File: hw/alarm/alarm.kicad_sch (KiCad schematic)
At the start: 23 parts, among them IC1 DS3231S#T&R, IC2 TSOP38238, IC3 SHT40-BD1B-R2, U1 RaspberryPi_Pico, U2 PEC11R-4215F-S0024, U4 HT16K33

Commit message: Reorganize libraries, various updates to schematic
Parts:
- removed D1: RB876WTL, symbol Device:D_Schottky
- removed LED3, LED4: DISP_SEGMENT_STARBURST_DUAL_COMMONCATHODE, Adafruit 0.54 Alphanumeric STEMMA QT:SEGMENT_STARTBUST_DUAL_KWA-541CBB, symbol Adafruit 0.54 Alphanumeric STEMMA QT-eagle-import:DISP_SEGMENT_STARBURST_DUAL_C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
- removed LS1, LS2, LS3: CEM-1203_42_, CEM-1203(42), symbol SamacSys_Parts:CEM-1203_42_
- removed U4: HT16K33, Adafruit 0.54 Alphanumeric STEMMA QT:SOP28_300MIL_SKINNY, symbol Adafruit 0.54 Alphanumeric STEMMA QT-eagle-import:HT16K33_SOP28_SKINNY
- added C10, C12, C16: 4.7uF, Capacitor_SMD:C_0805_2012Metric, symbol Device:C
- added C11, C13, C14, C15, C3, C4, C5, C6, C7, C8, C9: 0.1uF, Capacitor_SMD:C_0805_2012Metric, symbol Device:C
- added D2: LED, LED_SMD:LED_0603_1608Metric, symbol Device:LED
- added D3, D4, D5: MBR0530, Diode_SMD:D_SOD-123, symbol Diode:MBR0530
- added IC4: 23K256-I_SN, SOIC127P600X175-8N, symbol SamacSys_Parts:23K256-I_SN
- added J1: 4328, 4328:ADAFRUIT_4328, symbol 4328:4328
- added J2: SFV24R-4STBE1HLF, SFV24R4STBE1HLF, symbol SamacSys_Parts:SFV24R-4STBE1HLF
- added L1: 10uH, NR4018T100M, symbol SamacSys_Parts:NR4018T100M
- added LS1, LS2, LS3: PT-1241PFQ, PT1241PFQ, symbol SamacSys_Parts:PT-1241PFQ
- added Q1: DMG2305UX-7, SOT96P240X115-3N, symbol SamacSys_Parts:DMG2305UX-7
- added Q2: IRLML2060TRPBF, SOT95P237X112-3N, symbol SamacSys_Parts:IRLML2060TRPBF
- added R3: 267Ω, Resistor_SMD:R_0603_1608Metric_Pad0.98x0.95mm_HandSolder, symbol Device:R
- added U3: 2462, 2462, symbol SamacSys_Parts:2462
- added U4: AS1115-BSST, Package_SO:QSOP-24_3.9x8.7mm_P0.635mm, symbol Interface_Expansion:AS1115-BSST
- added U5: TDCR1060M, TDCG1060M_VIS, symbol 2024-07-15_04-25-04:TDCR1060M
- C1, C2: value 10uF -> 0.1uF; footprint (none) -> Capacitor_SMD:C_0805_2012Metric
- R1: value 10k -> 0.47Ω; footprint (none) -> Resistor_SMD:R_0603_1608Metric_Pad0.98x0.95mm_HandSolder
- R2: value 10k -> 10kΩ; footprint (none) -> Resistor_SMD:R_0603_1608Metric_Pad0.98x0.95mm_HandSolder
- U1: footprint Module_RaspberryPi_Pico:RaspberryPi_Pico_Common -> Module_RaspberryPi_Pico:RaspberryPi_Pico_Original_SMD_MountingHoles_HandSolder_Castellated; symbol MCU_Module_RaspberryPi_Pico:RaspberryPi_Pico -> MCU_Module_RaspberryPi_Pico:RaspberryPi_Pico_DebugPins
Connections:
- net +3.3V: now also IC2.3 (VS), IC3.4 (VSS), C10.2, C14.1, C15.1, C16.1, IC4.7 (~{HOLD}), IC4.8 (VCC), J1.4, J2.15 (VDDIO), J2.16 (VCI), L1.1
- net GND: now also IC2.2 (GND), IC3.3 (VDD), R1.2, R2.2, S2.3, S3.3, S4.3, S5.3, S6.3, S7.1 (COM), U1.D2 (GND), U2.1 (COM), U2.C1 (COMMON), C10.1, C11.1, C13.1, C14.2, C15.2, C16.2, C3.1, C4.1, C5.1, C6.1, C7.1, C8.1, C9.1, D2.1 (K), D3.1 (K), IC4.4 (VSS), J1.3, J2.17 (VSS), J2.8 (BSI), LS1.1 (-), LS2.1 (-), LS3.1 (-), U3.2 (-)
- net SCL: now also IC3.2 (SCL), U1.7 (GPIO5), J1.1; no longer R2.2, U1.27 (GPIO21)
- net SDA: now also IC3.1 (SDA), U1.6 (GPIO4), J1.2; no longer R1.2, U1.29 (GPIO22)
- net at S5.2: now also U1.20 (GPIO15)
- net at S4.2: now also U1.19 (GPIO14)
- net at S6.2: now also U1.15 (GPIO11)
- net at IC2.1 (OUT): now also U1.29 (GPIO22), R3.2
- net at S3.2: now also U1.17 (GPIO13)
- net MOSI: now reaches U1.1 (GPIO0)
- net MOSI: now also IC4.5 (SI), J2.14 (SDIO)
- net EinkCS: now reaches U1.10 (GPIO7)
- net EinkCS: now also J2.12 (CS)
- net Enc_A1: now reaches U1.11 (GPIO8)
- net Enc_A1: now also U2.A1 (CHANNEL_A)
- net Enc_B1: now reaches U1.12 (GPIO9)
- net Enc_B1: now also U2.B1 (CHANNEL_B)
- net at U1.14 (GPIO10): now also U2.2 (NO)
- net at U1.16 (GPIO12): now also S2.2
- net MISO: now reaches U1.2 (GPIO1)
- net MISO: now also IC4.2 (SO)
- net at U1.21 (GPIO16): now also LS3.2 (+)
- net at U1.22 (GPIO17): now also LS2.2 (+)
- net at U1.24 (GPIO18): now also LS1.2 (+)
- net at U1.25 (GPIO19): now also S7.2 (NO)
- net EinkRESET: now reaches U1.26 (GPIO20)
- net EinkRESET: now also J2.10 (RES)
- net at U1.39 (VSYS): now also Q1.2 (S)
- net SCK: now reaches U1.4 (GPIO2)
- net SCK: now also IC4.6 (SCK), J2.13 (SCK)
- net at U1.40 (VBUS): now also Q1.1 (G)
- net DC: now reaches U1.5 (GPIO3)
- net DC: now also J2.11 (D/C)
- net SRAMCS: now reaches U1.9 (GPIO6)
- net SRAMCS: now also IC4.1 (~{CS})
- net GDR: now reaches R2.1
- net GDR: now also J2.2 (GDR), Q2.1 (G); no longer R1.1
- new net: C8.2, J2.5 (VSH2)
- new net: C12.1, D5.2 (A), L1.2, Q2.3 (D)
- new net: C12.2, D3.2 (A), D4.1 (K)
- new net: C3.2, J2.24 (VCOM)
- new net: C6.2, J2.19 (VPP)
- new net: C5.2, J2.20 (VSH1)
- new net: D2.2 (A), R3.1
- new net: Q1.3 (D), U3.1 (+)
- new net: C7.2, J2.18 (VDD)
- new net: C4.2, J2.22 (VSL)
- new net: C9.2, J2.4 (VGL/NC)
- new net: J1.SH1 (SHIELD), J1.SH2 (SHIELD)
- new net EinkBUSY: J2.9 (BUSY), U1.27 (GPIO21)
- new net RESE: J2.3 (RESE), Q2.2 (S), R1.1
- new net VGH: C13.2, D5.1 (K), J2.21 (VGH)
- new net VGL: C11.2, D4.2 (A), J2.23 (VGL)
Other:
- note added: "E-paper"
- note added: "RTC"
- note added: "Temp/Humidity"
- moved on the sheet: IC1, IC2, IC3, S7

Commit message: Add segment display circuit
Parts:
- removed Q2: IRLML2060TRPBF, SOT95P237X112-3N, symbol SamacSys_Parts:IRLML2060TRPBF
- added C17: 0.1uF, Capacitor_SMD:C_0805_2012Metric, symbol Device:C
- added Q3: Si1308EDL-T1-GE3, SOT65P210X110-3N, symbol SamacSys_Parts:Si1308EDL-T1-GE3
- added R4: 10kΩ, Resistor_SMD:R_0603_1608Metric_Pad0.98x0.95mm_HandSolder, symbol Device:R
- added S8: PTS647SM70SMTR2LFS, PTS647SM38SMTR2LFS, symbol SamacSys_Parts:PTS647SM70SMTR2LFS
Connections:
- net +3.3V: now also U4.19 (VDD), C17.2, R4.1
- net GDR: now also Q3.1 (G)
- net GND: now also U4.6 (GND), C17.1; no longer S2.3, S3.3, S4.3, S5.3, S6.3
- net RESE: now also Q3.2 (S)
- net SCL: now also U4.14 (SCL)
- net SDA: now also U4.1 (SDA)
- net at C12.1, D5.2 (A), L1.2: now also Q3.3 (D)
- net at S5.2: now also U4.15 (SEGA), U5.14 (ANODE_A); no longer U1.20 (GPIO15)
- net at S4.2: now also U4.17 (SEGB), U5.16 (ANODE_B); no longer U1.19 (GPIO14)
- net at S6.2: now also U4.21 (SEGE), U5.5 (ANODE_E); no longer U1.15 (GPIO11)
- net KEYA: now reaches U4.11 (KEYA)
- net KEYA: now also S2.3, S3.3, S4.3, S5.3, S6.3, S8.1
- net at U4.13 (ISET): now also R4.2
- net at U4.16 (SEGF): now also U5.11 (ANODE_F), S8.2
- net at U4.18 (SEGG): now also U5.15 (ANODE_G)
- net at U4.2 (DIG0): now also U5.1 (CC_D1)
- net at U4.20 (SEGC): now also S3.2, U5.13 (ANODE_C)
- net at U4.22 (SEGDP): now also U5.7 (ANODE_DP)
- net at U4.23 (SEGD): now also S2.2, U5.3 (ANODE_D)
- net IRQ: now reaches U4.24 (IRQ)
- net IRQ: now also U1.15 (GPIO11)
- net at U4.3 (DIG1): now also U5.2 (CC_D2)
- net at U4.4 (DIG2): now also U5.4 (CC_L1_L2)
- net at U4.5 (DIG3): now also U5.6 (CC_D3)
- net at U4.7 (DIG4): now also U5.8 (CC_D4)
- net at U4.8 (DIG5): now also U5.10 (CC_L3)
- net ANODE_L1_L2: now reaches U1.17 (GPIO13)
- net ANODE_L1_L2: now also U5.12 (ANODE_L1_L2); no longer S3.2
- net ANODE_L3: now reaches U1.16 (GPIO12)
- net ANODE_L3: now also U5.9 (ANODE_L3); no longer S2.2
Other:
- note added: "Buttons"
- note added: "Pico"
- note added: "SRAM"
- note added: "Segment Display"
- note added: "Stemma-QT"
- note added: "https://files.waveshare.com/upload/4/4e/2.13inch_e-Paper_V4_Specification.pdf"
- moved on the sheet: C1, C10, C11, C12, C13, C14, C15, C16, C2, C3, C4, C5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

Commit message: Start board layout
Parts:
- removed L1: 10uH, NR4018T100M, symbol SamacSys_Parts:NR4018T100M
- removed U3: 2462, 2462, symbol SamacSys_Parts:2462
- added BT1: 2464, 2464, symbol SamacSys_Parts:2464
- added L1: 68 uH, INDM3225X240N, symbol SamacSys_Parts:CM322522-680KL
- C1, C11, C13, C14, C15, C17, C2, C3, C4, C5, C6, C7, C8, C9: value 0.1uF -> 1uF
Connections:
- net +3.3V: now also L1.1
- net GND: now also BT1.2 (-)
- net at C12.1, D5.2 (A), Q3.3 (D): now also L1.2
- net at Q1.3 (D): now also BT1.1 (+)

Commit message: Continue board layout
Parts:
- removed BT1: 2464, 2464, symbol SamacSys_Parts:2464
- removed U2: PEC11R-4215F-S0024, PEC11R4215FS0024, symbol SamacSys_Parts:PEC11R-4215F-S0024
- added IC5: PEC11S-929K-S0015, PEC11S929KS0015, symbol SamacSys_Parts:PEC11S-929K-S0015
- added U3: 2462, 2462, symbol SamacSys_Parts:2462
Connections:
- net Enc_A1: now also IC5.A1 (CCW)
- net Enc_B1: now also IC5.B1 (CW)
- net GND: now also IC5.C1 (WIPER), IC5.D1 (COM), U3.2 (-)
- net KEYA: now also S8.3; no longer S8.1
- net Enc_Switch: now reaches U1.14 (GPIO10)
- net Enc_Switch: now also IC5.E1 (NO)
- net at Q1.3 (D): now also U3.1 (+)
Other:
- note added: "Encoder"
- moved on the sheet: C15, IC3

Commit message: Finish board layout initial ver
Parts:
- removed LS1, LS2, LS3: PT-1241PFQ, PT1241PFQ, symbol SamacSys_Parts:PT-1241PFQ
- added LS1, LS2: CPT-9019A-SMT-TR, CPT-9019A_CUD, symbol CPT_9019A_SMT_TR:CPT-9019A-SMT-TR
- added TP1, TP2, TP3, TP4, TP5: TestPoint, TestPoint:TestPoint_Pad_1.0x1.0mm, symbol Connector:TestPoint
- U1: footprint Module_RaspberryPi_Pico:RaspberryPi_Pico_Original_SMD_MountingHoles_HandSolder_Castellated -> Module_RaspberryPi_Pico:RaspberryPi_Pico_Original_SMD; symbol MCU_Module_RaspberryPi_Pico:RaspberryPi_Pico_DebugPins -> MCU_Module_RaspberryPi_Pico:RaspberryPi_Pico_SecondaryPins
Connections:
- net GND: now also LS1.2, LS2.2
- net at U1.22 (GPIO17): now also LS2.1
- net at U1.21 (GPIO16): now also LS1.1
- new net: TP2.1, U1.TP2 (USB_DM)
- new net: TP1.1, U1.TP1 (USB_GND)
- new net: TP3.1, U1.TP3 (USB_DP)
- new net: TP4.1, U1.TP5 (LED_OUT)
- new net: TP5.1, U1.TP6 (~{BOOTSEL})

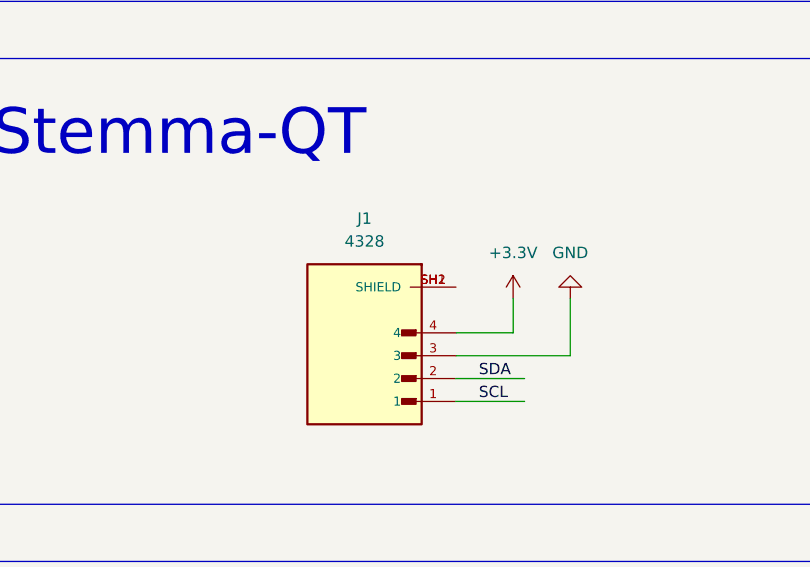
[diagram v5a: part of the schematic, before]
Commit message: Make DRC-rec'd changes
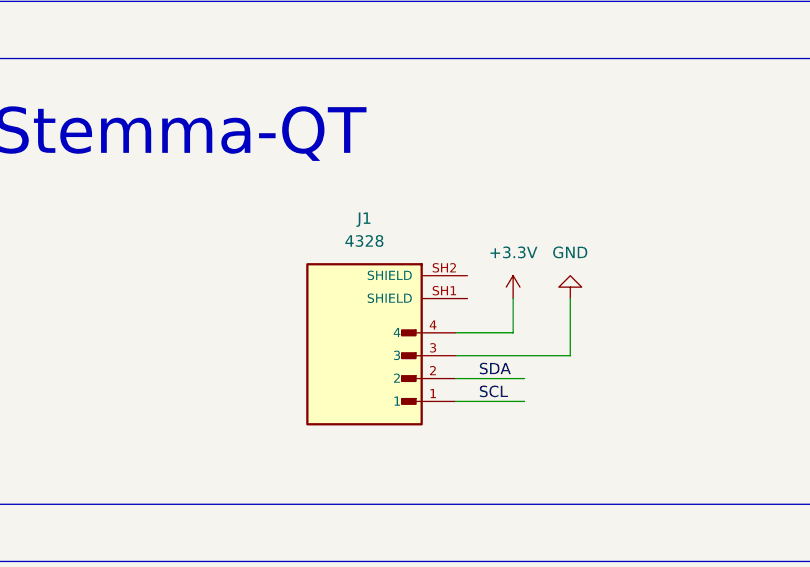
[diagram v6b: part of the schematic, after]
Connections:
- net at J1.SH1 (SHIELD): no longer J1.SH2 (SHIELD)

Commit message: Add pull-ups to i2c line, fix problems with DS3231 circuit
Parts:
- added R5, R6: 10kΩ, Resistor_SMD:R_0603_1608Metric_Pad0.98x0.95mm_HandSolder, symbol Device:R
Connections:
- net +3.3V: now also R5.1, R6.1; no longer IC1.14 (VBAT)
- net GND: now also IC1.10 (N.C._6), IC1.11 (N.C._7), IC1.12 (N.C._8), IC1.14 (VBAT), IC1.5 (N.C._1), IC1.6 (N.C._2), IC1.7 (N.C._3), IC1.8 (N.C._4), IC1.9 (N.C._5)
- net SCL: now also R6.2
- net SDA: now also R5.2

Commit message: Finish v2 schematic and begin v2 board layout
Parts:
- removed C14: 1uF, Capacitor_SMD:C_0805_2012Metric, symbol Device:C
- removed IC1: DS3231S#T&R, SOIC127P1032X265-16N, symbol SamacSys_Parts:DS3231S#T&R
- removed IC2: TSOP38238, TSOP38238, symbol SamacSys_Parts:TSOP38238
- removed IC4: 23K256-I_SN, SOIC127P600X175-8N, symbol SamacSys_Parts:23K256-I_SN
- removed LS1, LS2: CPT-9019A-SMT-TR, CPT-9019A_CUD, symbol CPT_9019A_SMT_TR:CPT-9019A-SMT-TR
- removed TP1, TP2, TP3, TP4, TP5: TestPoint, TestPoint:TestPoint_Pad_1.0x1.0mm, symbol Connector:TestPoint
- removed U3: 2462, 2462, symbol SamacSys_Parts:2462
- added A1: ~, RX480E:RX480E, symbol RX480E:RX480E
- added C18, C19: 1uF, Capacitor_SMD:C_0603_1608Metric, symbol Device:C
- added D1: MBR0530, Diode_SMD:D_SOD-123, symbol Diode:MBR0530
- added IC6: MAX31328NELB+, MAX31328NELB, symbol SamacSys_Parts:MAX31328NELB+
- added J3: 975, 975, symbol SamacSys_Parts:975
- added LS2: CSS-I4B20-SMT-TR, CSSI4B20SMTTR, symbol SamacSys_Parts:CSS-I4B20-SMT-TR
- added Q2: 2SC5585TL, 2SC5585TL, symbol SamacSys_Parts:2SC5585TL
- added Q4: DMG2305UX-7, SOT96P240X115-3N, symbol SamacSys_Parts:DMG2305UX-7
- added R10, R11, R12, R14, R8, R9: 10kΩ, Resistor_SMD:R_0603_1608Metric_Pad0.98x0.95mm_HandSolder, symbol Device:R
- added R13, R7: 130Ω, Resistor_SMD:R_0603_1608Metric_Pad0.98x0.95mm_HandSolder, symbol Device:R
- added R15: 47Ω, Resistor_SMD:R_0603_1608Metric_Pad0.98x0.95mm_HandSolder, symbol Device:R
- added R16: 180Ω, Resistor_SMD:R_0603_1608Metric_Pad0.98x0.95mm_HandSolder, symbol Device:R
- added S9: PTS647SM70SMTR2LFS, PTS647SM38SMTR2LFS, symbol SamacSys_Parts:PTS647SM70SMTR2LFS
- C1: value 1uF -> 4.7uF; footprint Capacitor_SMD:C_0805_2012Metric -> Capacitor_SMD:C_0603_1608Metric
- C10, C11, C12, C13, C15, C16, C17, C2, C3, C4, C5, C6, C7, C8, C9: footprint Capacitor_SMD:C_0805_2012Metric -> Capacitor_SMD:C_0603_1608Metric
- D2: footprint LED_SMD:LED_0603_1608Metric -> SamacSys_Parts:WP710A10LID
- J2: value SFV24R-4STBE1HLF -> FFC2B35-24-T; footprint SFV24R4STBE1HLF -> FFC2B3524T; symbol SamacSys_Parts:SFV24R-4STBE1HLF -> SamacSys_Parts:FFC2B35-24-T; Height 2 -> 2.2; Manufacturer_Name Amphenol -> GCT (GLOBAL CONNECTOR TECHNOLOGY); Manufacturer_Part_Number SFV24R-4STBE1HLF -> FFC2B35-24-T; Mouser Part Number 649-SFV24R-4STBE1HLF -> 640-FFC2B35-24-T; Mouser Price/Stock https://www.mouser.co.uk/ProductDetail/Amphenol-FCI/SFV24R-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 -> https://www.mouser.co.uk/ProductDetail/GCT/FFC2B35-24-T?qs=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
- R3: value 267Ω -> 1kΩ
- R4: value 10kΩ -> 13.9kΩ
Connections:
- net +3.3V: now also C1.2, IC3.3 (VDD), J1.2, R3.2, A1.2 (+3.3V), D1.1 (K), IC6.2 (VCC), LS2.1 (+_1), LS2.4 (+_2), R11.1, R12.1, R14.1, R8.1; no longer C1.1, IC3.4 (VSS), J1.4
- net DC: now also U1.27 (GPIO21); no longer U1.5 (GPIO3)
- net EinkBUSY: now also U1.22 (GPIO17); no longer U1.27 (GPIO21)
- net EinkRESET: now also U1.21 (GPIO16); no longer U1.26 (GPIO20)
- net Enc_A1: now also R9.1; no longer IC5.A1 (CCW)
- net Enc_B1: now also R10.2; no longer IC5.B1 (CW)
- net GND: now also C1.1, IC3.4 (VSS), J1.1, A1.1 (GND), C18.1, C19.1, IC6.5 (N.C._1), IC6.6 (N.C._2), IC6.7 (GND), IC6.8 (VBAT), J3.1 (-), Q2.1 (E), Q4.1 (G), R13.1, R7.1; no longer C1.2, IC3.3 (VDD), IC5.D1 (COM), J1.3
- net IRQ: now also R8.2
- net MISO: now also U1.26 (GPIO20); no longer U1.2 (GPIO1)
- net MOSI: now also U1.25 (GPIO19); no longer U1.1 (GPIO0)
- net SCK: now also U1.24 (GPIO18); no longer U1.4 (GPIO2)
- net SCL: now also J1.4, IC6.10 (SCL); no longer J1.1
- net SDA: now also J1.3, IC6.9 (SDA); no longer J1.2
- net at U4.18 (SEGG), U5.15 (ANODE_G): now also S9.2
- net Enc_E: now reaches U4.22 (SEGDP), U5.7 (ANODE_DP)
- net Enc_E: now also IC5.E1 (NO)
- net at U5.4 (CC_L1_L2): now also R13.2; no longer U4.4 (DIG2)
- net at U5.6 (CC_D3): now also U4.4 (DIG2); no longer U4.5 (DIG3)
- net at U5.8 (CC_D4): now also U4.5 (DIG3); no longer U4.7 (DIG4)
- net at U5.10 (CC_L3): now also R7.2; no longer U4.8 (DIG5)
- net at U1.29 (GPIO22): no longer R3.2
- net at D2.2 (A): now also R15.1; no longer R3.1
- net RTC_INT: now reaches U1.19 (GPIO14)
- net RTC_INT: now also IC6.3 (~{INT}/SQW), R14.2
- net Buzzer: now reaches U1.20 (GPIO15)
- net Buzzer: now also R16.1
- net at S7.2 (NO): now also U1.14 (GPIO10); no longer U1.25 (GPIO19)
- net at Q1.3 (D): now also Q4.2 (S)
- removed net Enc_Switch: IC5.E1 (NO), U1.14 (GPIO10)
- net KEYA renamed Enc_D
- net Enc_D: now also IC5.D1 (COM), S9.3
- net SRAMCS: no longer names the net of U1.9 (GPIO6)
- new net: C19.2, IC5.A1 (CCW), R11.2, R9.2
- new net: D1.2 (A), LS2.2 (-_1), LS2.3 (-_2), Q2.3 (C)
- new net: C18.2, IC5.B1 (CW), R10.1, R12.2
- new net: Q2.2 (B), R16.2
- new net: J3.3 (+), Q4.3 (D)
- new net RF1: A1.3 (OUT1), U1.5 (GPIO3)
- new net RF_key: A1.7 (KEY), R15.2, R3.1, U1.4 (GPIO2)
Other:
- note added: "Buzzer"
- note added: "Ideal OR"
- note added: "Receiver"
- note added: "Reset"
- note added: "Reverse Polarity Protection"
- note removed: "SRAM"
- moved on the sheet: C10, C11, C12, C13, C15, C16, C17, C2, C3, C4, C5, C6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
